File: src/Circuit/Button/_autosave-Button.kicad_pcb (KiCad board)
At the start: 2 copper layers, 3 parts

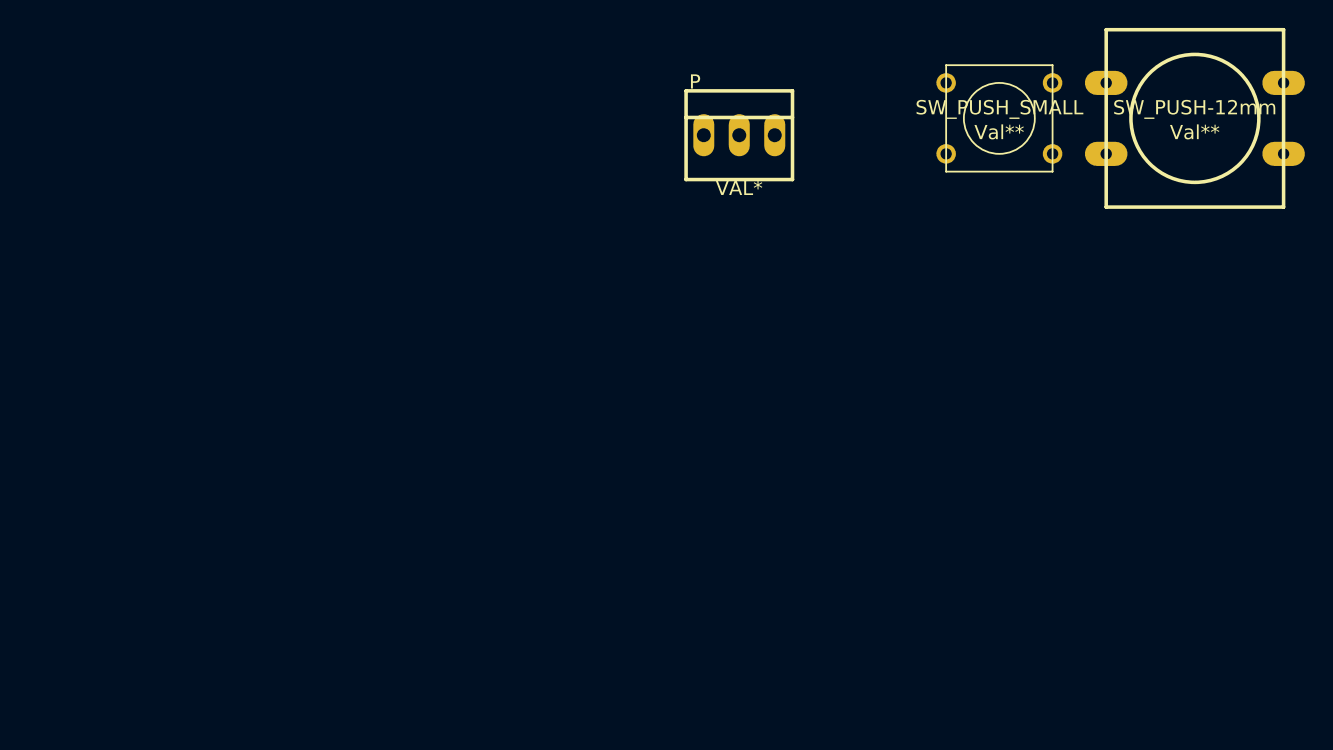
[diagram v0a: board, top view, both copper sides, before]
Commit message: Generated gerber files for button PCB
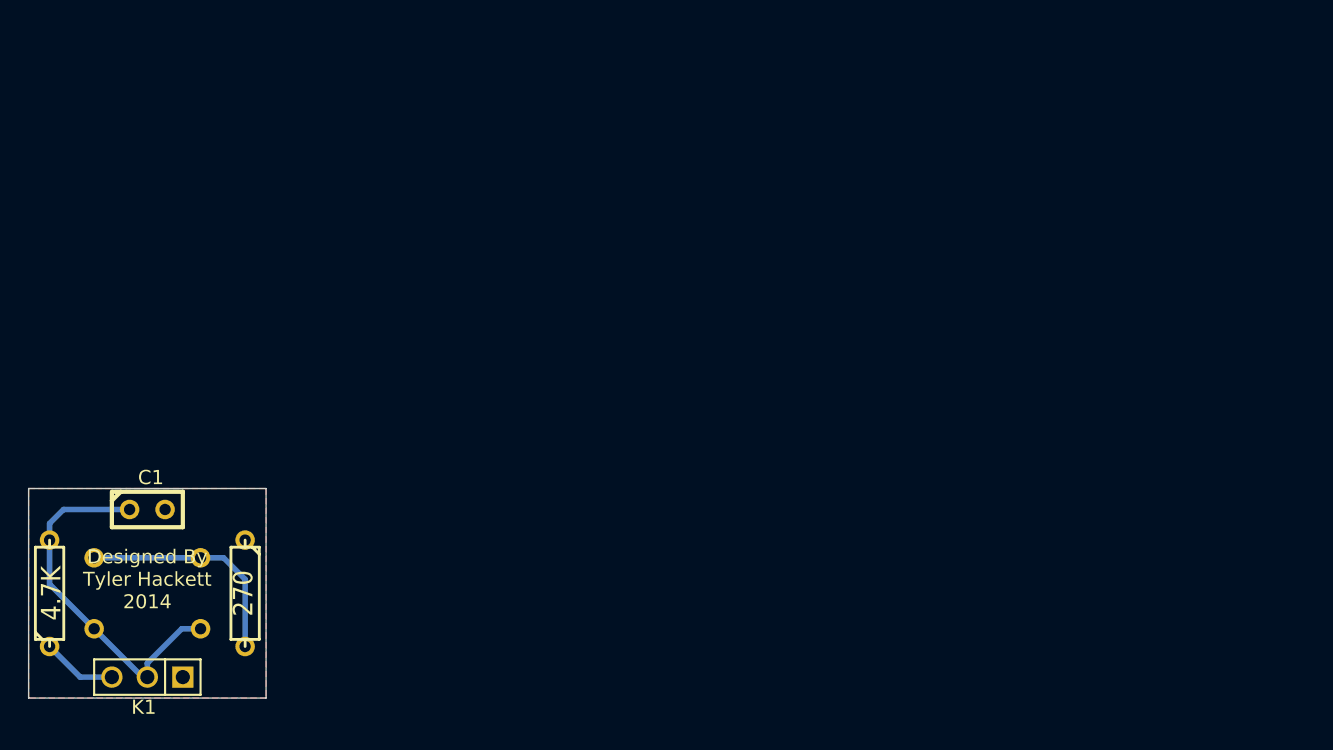
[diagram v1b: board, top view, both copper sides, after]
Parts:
- removed P: VAL*, PINHEAD1-3
- removed SW_PUSH-12mm: Val**, SW_PUSH-12mm
- removed SW_PUSH_SMALL: Val**, SW_PUSH_SMALL
- added C1: 10nF, C1, F.Cu at (204.0, 135.0)
- added K1: CONN_3, PIN_ARRAY_3X1, F.Cu at (204.0, 147.0)
- added R1: 4.7K, R3, F.Cu at (197.0, 141.0)
- added R2: 270, R3, F.Cu at (211.0, 141.0)
- added SW1: SW_PUSH, SW_PUSH_SMALL, B.Cu at (204.0, 141.0)
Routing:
- net N-000002: track 0.00 -> 26.1 mm
- net N-000001: track 0.00 -> 16.3 mm
- net VCC: track 0.00 -> 5.37 mm
- added copper zone on F.Cu, net GND
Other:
- board outline added: 17 x 15 mm
- net class Default: trace_width 0.254 -> 0.4
- board text added: "Designed By Tyler Hackett 2014"
